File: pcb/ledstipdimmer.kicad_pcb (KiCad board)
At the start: 2 copper layers, 20 x 38 mm, 44 parts, among them P1 SolderCable, P2 SolderCable, Q1 NTTFS5820NLTAG, Q2 NTTFS5820NLTAG, U1 TPS7B6950, U2 IQS904D

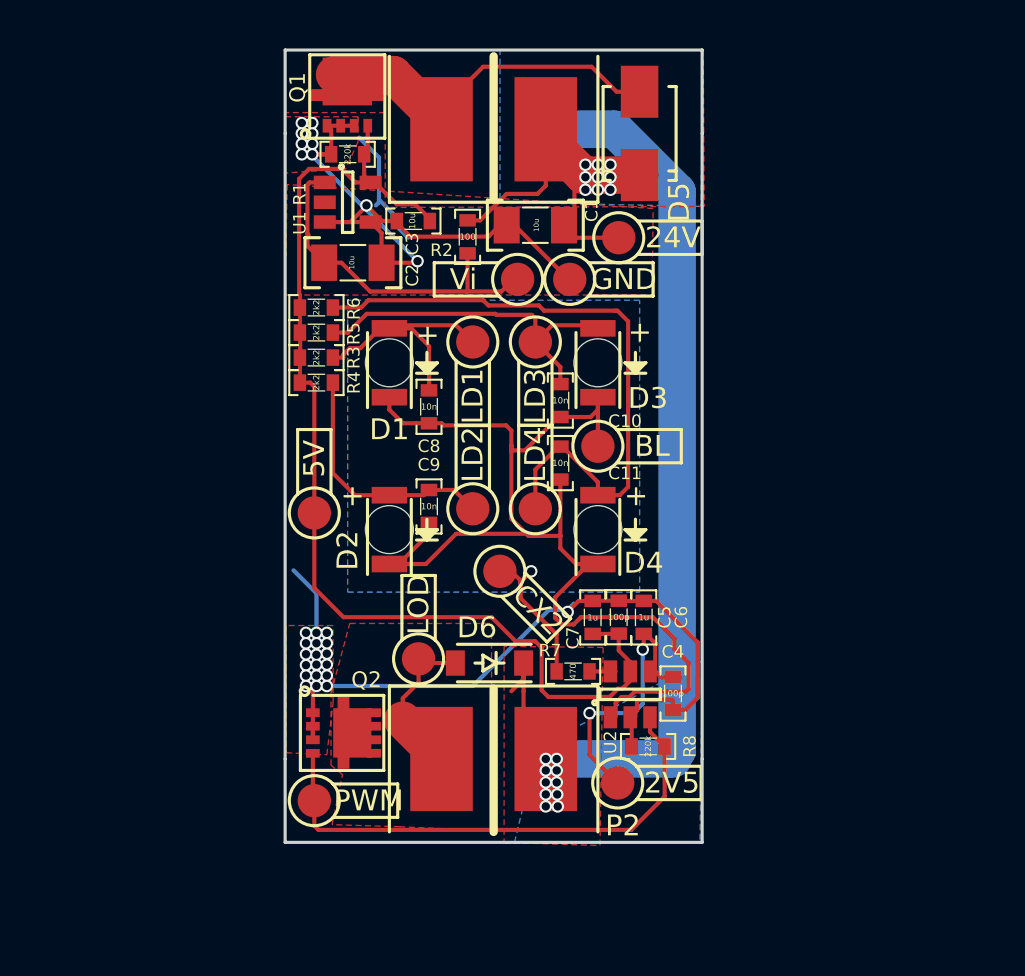
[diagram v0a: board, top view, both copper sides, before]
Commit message: Resolved DRC conflicts. Adjustments left.
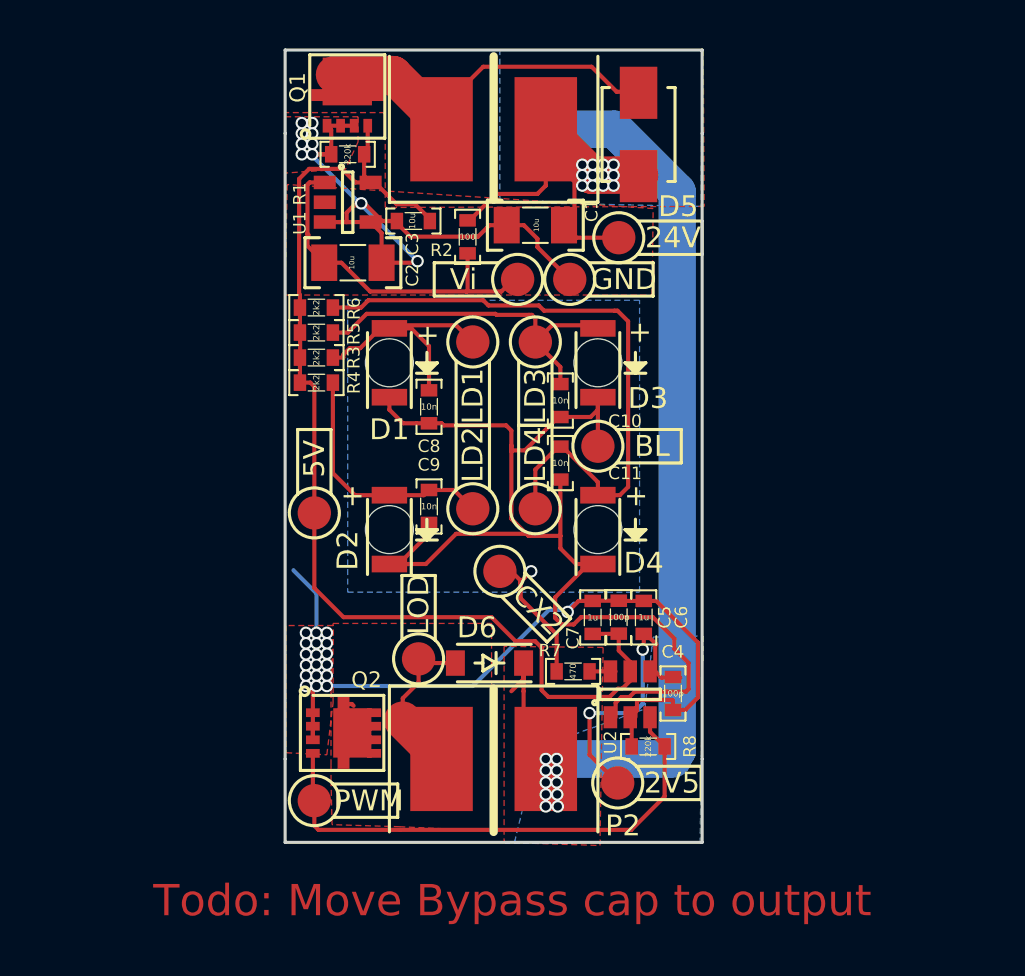
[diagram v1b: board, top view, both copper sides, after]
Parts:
- D5: footprint Diodes_SMD:SMA_Standard -> Diodes_SMD:SMA_Bipolar
- moved D5 0.07 mm to (77.0, 35.0)
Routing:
- net +24V: track 68.9 -> 76.0 mm, vias 15 -> 22
- net (no net): track 6.11 -> 0.00 mm, vias 4 -> 0
- net /LOAD: track 7.73 -> 10.6 mm
- net GND: track 87.3 -> 88.8 mm
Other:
- board text added: "Todo: Move Bypass cap to output"

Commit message: Produced panel and corresponding gerber files.
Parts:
- removed D5: SMAJ28CA, Diodes_SMD:SMA_Bipolar
- added REF**: manufacturing-breakaway, mhstuff:manufacturing-breakaway2, F.Cu at (76.0, 69.0)
- added REF**: manufacturing-breakaway, mhstuff:manufacturing-breakaway2, F.Cu at (64.0, 69.0)
- added REF**: manufacturing-breakaway, mhstuff:manufacturing-breakaway2, F.Cu at (80.0, 61.6)
- added REF**: manufacturing-breakaway, mhstuff:manufacturing-breakaway2, F.Cu at (60.0, 61.6)
- added REF**: manufacturing-breakaway, mhstuff:manufacturing-breakaway2, F.Cu at (80.0, 38.4)
- added REF**: manufacturing-breakaway, mhstuff:manufacturing-breakaway2, F.Cu at (60.0, 38.4)
- added REF**: manufacturing-breakaway, mhstuff:manufacturing-breakaway2, F.Cu at (64.0, 31.0)
- added REF**: manufacturing-breakaway, mhstuff:manufacturing-breakaway2, F.Cu at (76.0, 31.0)
- moved C1 19.8 mm to (68.2, 58.8)
- moved W14 2.50 mm to (63.9, 60.2)
- moved W1 2.39 mm to (73.6, 39.6)
- moved D6 0.80 mm to (69.8, 61.2)
- moved R3 0.75 mm to (62.2, 45.8)
- moved R4 0.75 mm to (62.2, 47.0)
- moved R5 0.75 mm to (62.2, 44.5)
- moved R6 0.75 mm to (62.2, 43.4)
- moved Q1 0.70 mm to (63.5, 33.4)
- moved R1 0.59 mm to (63.5, 36.3)
- moved C2 0.52 mm to (63.5, 41.7)
- moved U1 0.50 mm to (63.0, 38.8)
- moved C3 0.31 mm to (66.5, 39.2)
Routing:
- net /PWRm: track 17.9 -> 3.83 mm
- net +5V: track 53.3 -> 62.8 mm
- net /BL: track 57.0 -> 52.4 mm, vias 0 -> 2
- net /LOAD: track 10.6 -> 14.5 mm
- net /LD4: track 30.9 -> 28.8 mm
- net +2V5: track 13.5 -> 15.3 mm
- net /Touch: track 7.29 -> 8.93 mm
- net +24V: track 76.0 -> 74.7 mm
- net PWM: track 25.0 -> 23.8 mm
- net /LD3: track 17.2 -> 16.5 mm
- net GND: track 88.8 -> 88.7 mm, vias 29 -> 37
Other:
- outline, holes or cut-outs redrawn
- board text added: "QC"
- board text added: "rc0 Jan. 2017"
- board text removed: "Todo: Move Bypass cap to output"
